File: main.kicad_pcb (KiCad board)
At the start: 2 copper layers, 268.1 x 124.6 mm, 117 parts, among them SW1 Kailh-Choc, SW10 Kailh-Choc, SW11 Kailh-Choc, SW12 Kailh-Choc, SW13 Kailh-Choc, SW14 Kailh-Choc, SW15 Kailh-Choc, SW16 Kailh-Choc, SW17 Kailh-Choc, SW18 Kailh-Choc, SW19 Kailh-Choc, SW2 Kailh-Choc, SW20 Kailh-Choc, SW21 Kailh-Choc, SW22 Kailh-Choc, SW23 Kailh-Choc, SW24 Kailh-Choc, SW25 Kailh-Choc, SW26 Kailh-Choc, SW27 Kailh-Choc, SW28 Kailh-Choc, SW29 Kailh-Choc, SW3 Kailh-Choc, SW30 Kailh-Choc, SW31 Kailh-Choc, SW32 Kailh-Choc, SW33 Kailh-Choc, SW34 Kailh-Choc, SW35 Kailh-Choc, SW36 Kailh-Choc, SW37 Kailh-Choc, SW38 Kailh-Choc, SW39 Kailh-Choc, SW4 Kailh-Choc, SW40 Kailh-Choc, SW5 Kailh-Choc, SW6 Kailh-Choc, SW7 Kailh-Choc, SW8 Kailh-Choc, SW9 Kailh-Choc, U1 nice_nano, U2 nice_nano

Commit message: Added vias and copper fill
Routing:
- net R_ROW3: track 188.7 -> 207.4 mm
- net GND: vias 3 -> 21

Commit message: Version 0.1.0
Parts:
- removed kibuzzard-63659328: G***, kibuzzard-63659328
- removed kibuzzard-63703FC3: G***, kibuzzard-63703FC3
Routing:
- net R_ROW2: track 126.6 -> 125.2 mm
- net COL1: track 163.1 -> 162.1 mm
- net R_COL4: track 175.8 -> 175.0 mm
- net Net-(D16-A): track 3.76 -> 3.20 mm
- net GND: vias 21 -> 22
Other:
- board text added: "Brain 0.1.0"
- board text added: "Brain is based on: Urchin by duckyb, which is based on Sweep by davidphilipbarr, and Swoop by jimmerrick, which is based on Ferris by pierrechevalier83"
- board text added: "GITHUB.COM/WESZTMAN"

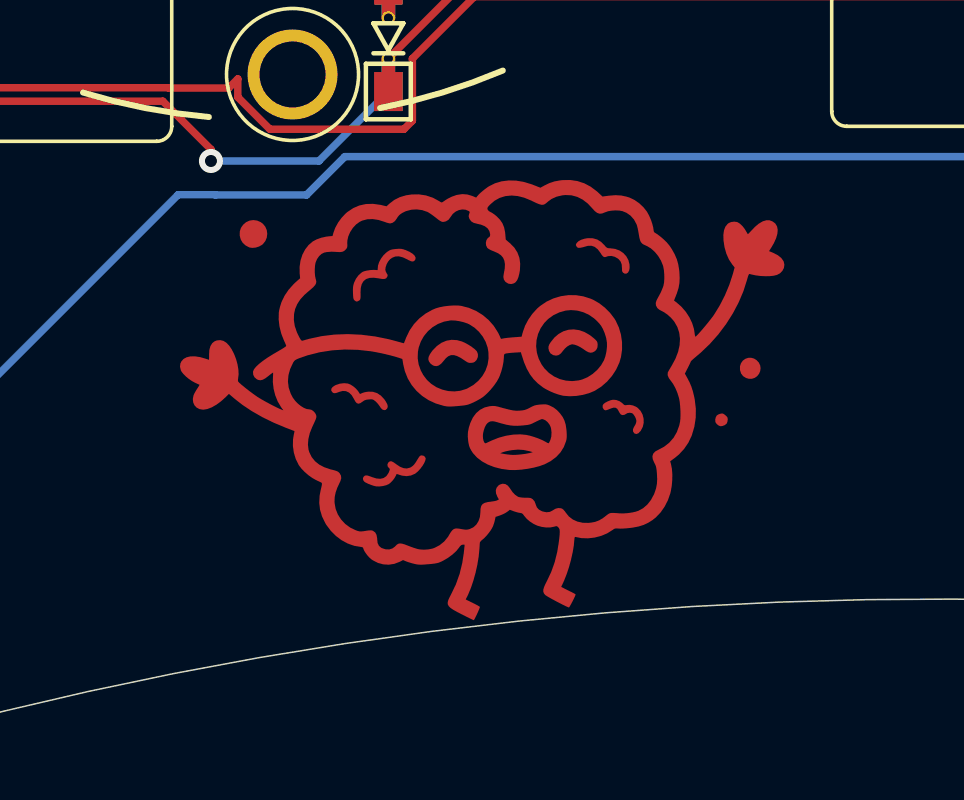
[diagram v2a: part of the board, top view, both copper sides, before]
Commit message: Changed icon to silkscreen
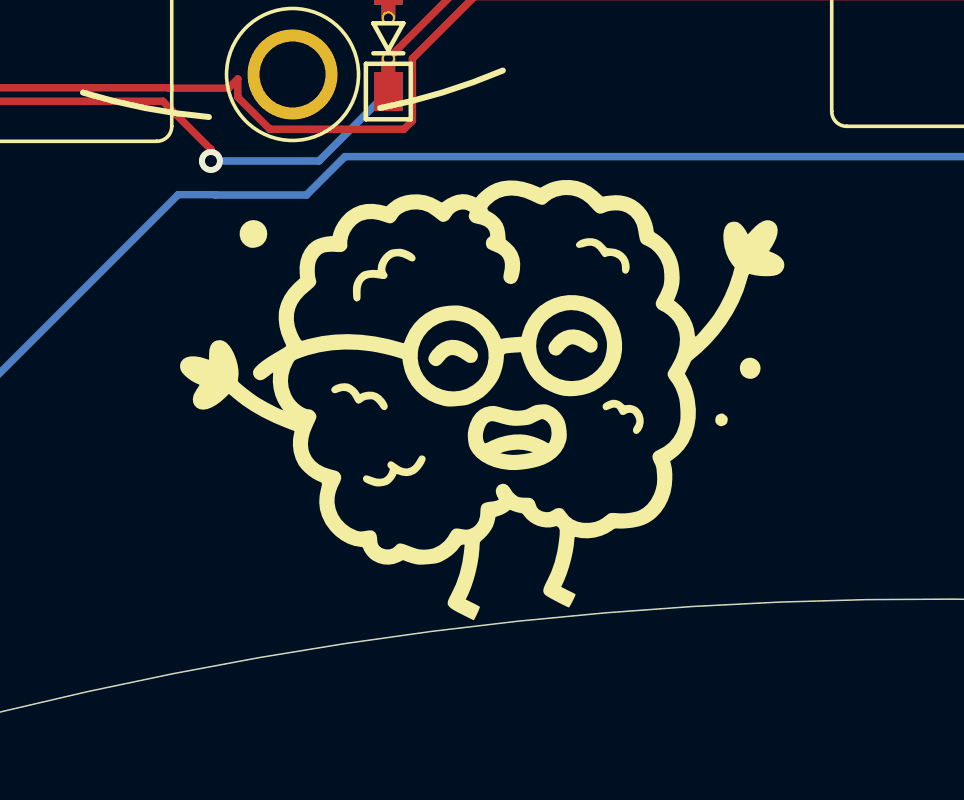
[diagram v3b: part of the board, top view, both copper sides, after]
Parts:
- removed the G*** at (280.4, 177.8)
- added G***: brain_silk, urchin-footprints:brain_silk, F.Cu at (280.4, 177.8)
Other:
- board text added: "Brain 0.2.0"
- board text removed: "Brain 0.1.0"

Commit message: Changed icon to silkscreen
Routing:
- net R_COL4: track 175.0 -> 174.4 mm
